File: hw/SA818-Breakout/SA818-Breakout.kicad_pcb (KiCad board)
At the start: 2 copper layers, 66 x 53 mm, 32 parts, among them J1 Conn_Coaxial, J2 Conn_01x02, J3 Conn_01x10, Q1 BSS138, Q2 BSS138, Q3 BSS138, Q4 BSS138, U10 NCP1117-5.0_SOT223, U11 NCP1117-3.3_SOT223

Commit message: Updating PCB
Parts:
- removed C3: 22u, Capacitor_SMD:C_0805_2012Metric_Pad1.18x1.45mm_HandSolder
- removed Q1, Q2, Q3, Q4: BSS138, Package_TO_SOT_SMD:SOT-23
- removed R1, R2, R3, R4, R5, R6, R7, R8: 10k, Resistor_SMD:R_0805_2012Metric_Pad1.20x1.40mm_HandSolder
- removed R10: 4.7, Resistor_SMD:R_0805_2012Metric_Pad1.20x1.40mm_HandSolder
- removed TP9: TestPoint, TestPoint:TestPoint_Pad_2.5x2.5mm
- removed U11: NCP1117-3.3_SOT223, Package_TO_SOT_SMD:SOT-223-3_TabPin2
- moved TP1 35.4 mm to (144.0, 91.0)
- moved J3 11.1 mm to (155.0, 98.8)
- moved H2 10.8 mm to (154.0, 91.0)
- moved H4 10.0 mm to (154.0, 130.0)
- moved TP8 7.24 mm to (139.0, 91.0)
- moved J2 5.99 mm to (143.0, 131.0)
- moved C1 5.17 mm to (130.8, 89.7)
- moved R9 5.17 mm to (130.8, 92.7)
- moved C2 5.17 mm to (134.8, 92.7)
- moved U10 5.17 mm to (122.8, 91.7)
- moved C5 4.00 mm to (148.0, 121.0)
- moved C6 4.00 mm to (148.0, 126.0)
- moved H1 4.00 mm to (108.0, 91.0)
- moved U1 0.47 mm to (138.5, 98.8)
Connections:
- C5 pad 1: PTT_5 -> PTT_3
- C6 pad 1: AFSQ_5 -> AFSQ_3
- U1 pad 1: AFSQ_5 -> AFSQ_3
- U1 pad 16: RXD_5 -> RXD_3
- U1 pad 17: TXD_5 -> TXD_3
- U1 pad 5: PTT_5 -> PTT_3
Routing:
- net +3.3V: track 78.9 -> 0.00 mm, vias 2 -> 0
- net AFSQ_5: track 49.6 -> 0.00 mm, vias 2 -> 0
- net RXD_5: track 40.4 -> 0.00 mm
- net TXD_5: track 40.3 -> 0.00 mm
- net +5V: track 106.1 -> 69.4 mm, vias 6 -> 2
- net AFSQ_3: track 11.5 -> 43.7 mm, vias 0 -> 2
- net RXD_3: track 9.45 -> 39.2 mm
- net TXD_3: track 10.4 -> 40.0 mm
- net +12V: track 60.5 -> 39.0 mm
- net PTT_5: track 18.2 -> 0.00 mm
- net AF_OUT: track 31.4 -> 17.1 mm
- net PTT_3: track 10.5 -> 20.0 mm
- net AF_IN: track 49.4 -> 39.9 mm
- net Net-(C3-Pad1): track 1.96 -> 0.00 mm
- net Net-(J2-Pin_1): track 9.25 -> 7.41 mm
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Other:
- board size 66 x 53 mm -> 56 x 49 mm

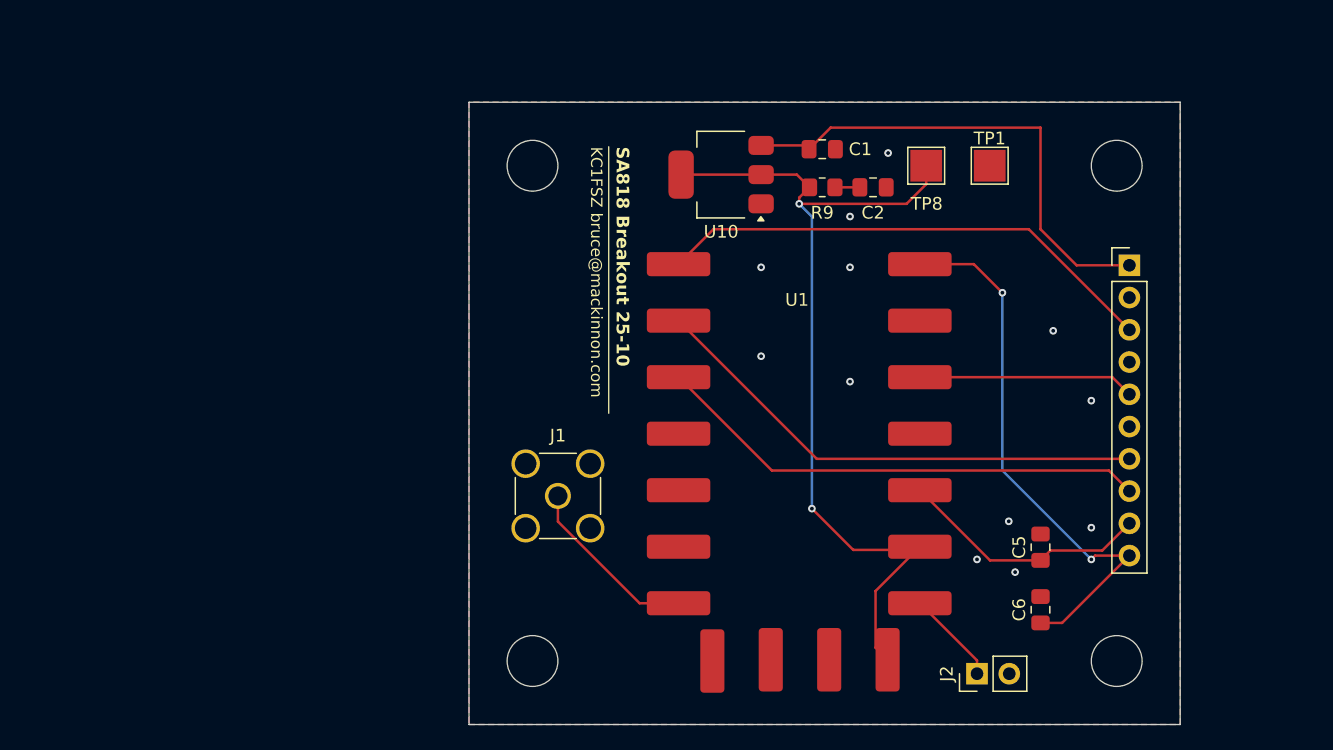
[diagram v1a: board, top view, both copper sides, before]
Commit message: Added LPF for harmonics
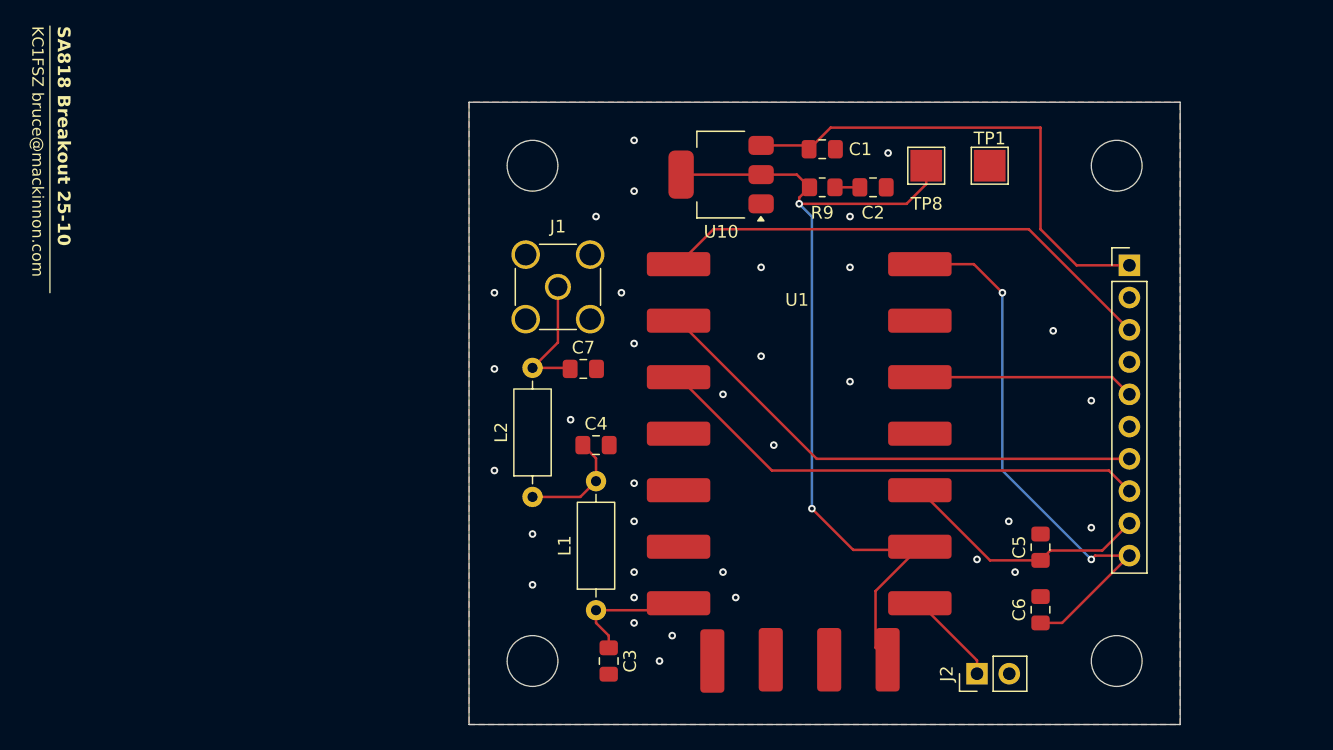
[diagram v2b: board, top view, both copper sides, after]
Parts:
- added C3: C_Small_US, Capacitor_SMD:C_0805_2012Metric_Pad1.18x1.45mm_HandSolder, F.Cu at (114.0, 130.0)
- added C4: C_Small_US, Capacitor_SMD:C_0805_2012Metric_Pad1.18x1.45mm_HandSolder, F.Cu at (113.0, 113.0)
- added C7: C_Small_US, Capacitor_SMD:C_0805_2012Metric_Pad1.18x1.45mm_HandSolder, F.Cu at (112.0, 107.0)
- added L1: L_Iron, Inductor_THT:L_Axial_L6.6mm_D2.7mm_P10.16mm_Horizontal_Vishay_IM-2, F.Cu at (113.0, 126.0)
- added L2: L_Iron, Inductor_THT:L_Axial_L6.6mm_D2.7mm_P10.16mm_Horizontal_Vishay_IM-2, F.Cu at (108.0, 117.1)
- moved J1 16.5 mm to (110.0, 100.5)
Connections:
- U1 pad 12: Net-(J1-In) -> ANT
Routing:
- net ANT: track 0.00 -> 10.1 mm
- net Net-(C4-Pad1): track 0.00 -> 8.78 mm
- net Net-(J1-In): track 14.2 -> 10.2 mm
- net GND: vias 12 -> 34
